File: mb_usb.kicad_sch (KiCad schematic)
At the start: 51 parts, among them J11 USB_A_Stacked, J8 USB_A_Stacked, J9 USB_C_Receptacle_USB2.0, U7 USB3320, U8 TPS2051BDBV, U9 GL850G, Y1 24Mhz, Y2 12Mhz

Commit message: update sch&layout
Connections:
- net H_DM renamed H_DN
- net H_DM1 renamed 1H_DN
- net H_DM2 renamed 2H_DN
- net H_DM3 renamed 3H_DN
- net H_DM4 renamed 4H_DN
- net H_DP1 renamed 1H_DP
- net H_DP2 renamed 2H_DP
- net H_DP3 renamed 3H_DP
- net H_DP4 renamed 4H_DP
- net S_DM renamed S_DN
- net USB_DM renamed USB_DN
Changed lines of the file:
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@@
     (stroke (width 0) (type default) (color 0 0 0 0))
   )
-  (label "H_DP4" (at 90.17 140.97 180)
+  (label "4H_DP" (at 90.17 140.97 180)
     (effects (font (size 1.27 1.27)) (justify right bottom))
   )
@@
     (effects (font (size 1.27 1.27)) (justify right bottom))
   )
-  (label "S_DM" (at 240.03 130.81 0)
+  (label "S_DN" (at 240.03 130.81 0)
     (effects (font (size 1.27 1.27)) (justify left bottom))
   )
-  (label "USB_DM" (at 151.13 70.485 180)
+  (label "USB_DN" (at 151.13 70.485 180)
     (effects (font (size 1.27 1.27)) (justify right bottom))
   )
-  (label "H_DP1" (at 90.17 121.92 180)
+  (label "1H_DP" (at 90.17 121.92 180)
     (effects (font (size 1.27 1.27)) (justify right bottom))
   )
@@
     (effects (font (size 1.27 1.27)) (justify left bottom))
   )
-  (label "H_DM" (at 130.175 70.485 0)
+  (label "H_DN" (at 130.175 70.485 0)
     (effects (font (size 1.27 1.27)) (justify left bottom))
   )
-  (label "USB_DM" (at 91.44 69.85 180)
+  (label "USB_DN" (at 91.44 69.85 180)
     (effects (font (size 1.27 1.27)) (justify right bottom))
   )
-  (label "H_DM2" (at 221.615 41.91 0)
+  (label "2H_DN" (at 221.615 41.91 0)
     (effects (font (size 1.27 1.27)) (justify left bottom))
   )
@@
     (effects (font (size 1.27 1.27)) (justify left bottom))
   )
-  (label "H_DM1" (at 221.615 36.83 0)
+  (label "1H_DN" (at 221.615 36.83 0)
     (effects (font (size 1.27 1.27)) (justify left bottom))
   )
-  (label "H_DM4" (at 90.17 143.51 180)
+  (label "4H_DN" (at 90.17 143.51 180)
     (effects (font (size 1.27 1.27)) (justify right bottom))
   )
@@
     (effects (font (size 1.27 1.27)) (justify right bottom))
   )
-  (label "S_DM" (at 130.175 64.135 0)
+  (label "S_DN" (at 130.175 64.135 0)
     (effects (font (size 1.27 1.27)) (justify left bottom))
   )
@@
     (effects (font (size 1.27 1.27)) (justify right bottom))
   )
-  (label "H_DP4" (at 220.98 88.265 0)
+  (label "4H_DP" (at 220.98 88.265 0)
     (effects (font (size 1.27 1.27)) (justify left bottom))
   )
@@
     (effects (font (size 1.27 1.27)) (justify right bottom))
   )
-  (label "H_DM" (at 52.07 124.46 0)
+  (label "H_DN" (at 52.07 124.46 0)
     (effects (font (size 1.27 1.27)) (justify left bottom))
   )
@@
     (effects (font (size 1.27 1.27)) (justify left bottom))
   )
-  (label "H_DM2" (at 90.17 130.81 180)
+  (label "2H_DN" (at 90.17 130.81 180)
     (effects (font (size 1.27 1.27)) (justify right bottom))
   )
@@
     (effects (font (size 1.27 1.27)) (justify right bottom))
   )
-  (label "H_DM1" (at 90.17 124.46 180)
+  (label "1H_DN" (at 90.17 124.46 180)
     (effects (font (size 1.27 1.27)) (justify right bottom))
   )
@@
     (effects (font (size 1.27 1.27)) (justify left bottom))
   )
-  (label "H_DM3" (at 90.17 137.16 180)
+  (label "3H_DN" (at 90.17 137.16 180)
     (effects (font (size 1.27 1.27)) (justify right bottom))
   )
@@
     (effects (font (size 1.27 1.27)) (justify right bottom))
   )
-  (label "H_DP2" (at 90.17 128.27 180)
+  (label "2H_DP" (at 90.17 128.27 180)
     (effects (font (size 1.27 1.27)) (justify right bottom))
   )
@@
     (effects (font (size 1.27 1.27)) (justify left bottom))
   )
-  (label "H_DP3" (at 220.98 83.185 0)
+  (label "3H_DP" (at 220.98 83.185 0)
     (effects (font (size 1.27 1.27)) (justify left bottom))
   )
-  (label "H_DM4" (at 220.98 90.805 0)
+  (label "4H_DN" (at 220.98 90.805 0)
     (effects (font (size 1.27 1.27)) (justify left bottom))
   )
-  (label "H_DP1" (at 221.615 34.29 0)
+  (label "1H_DP" (at 221.615 34.29 0)
     (effects (font (size 1.27 1.27)) (justify left bottom))
   )
-  (label "H_DM3" (at 220.98 85.725 0)
+  (label "3H_DN" (at 220.98 85.725 0)
     (effects (font (size 1.27 1.27)) (justify left bottom))
   )
@@
     (effects (font (size 1.27 1.27)) (justify right bottom))
   )
-  (label "H_DP3" (at 90.17 134.62 180)
+  (label "3H_DP" (at 90.17 134.62 180)
     (effects (font (size 1.27 1.27)) (justify right bottom))
   )
-  (label "H_DP2" (at 221.615 39.37 0)
+  (label "2H_DP" (at 221.615 39.37 0)
     (effects (font (size 1.27 1.27)) (justify left bottom))
   )

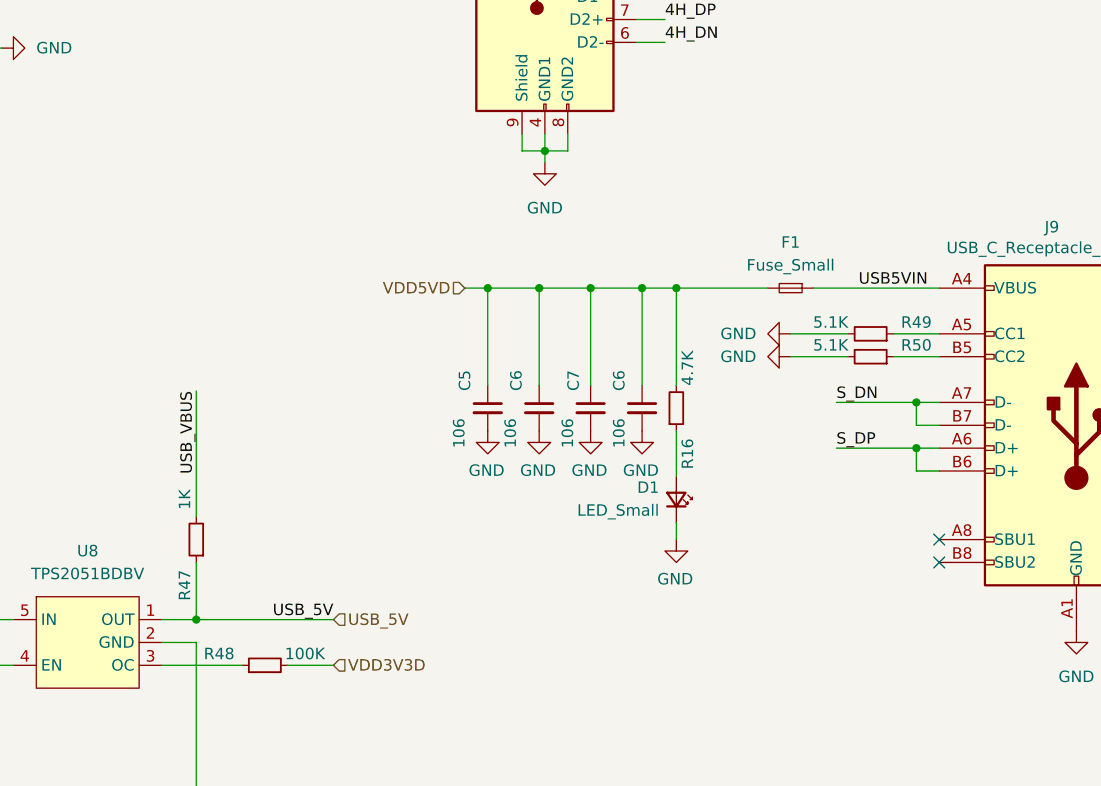
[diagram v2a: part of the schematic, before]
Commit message: Finall version --fix USB bug
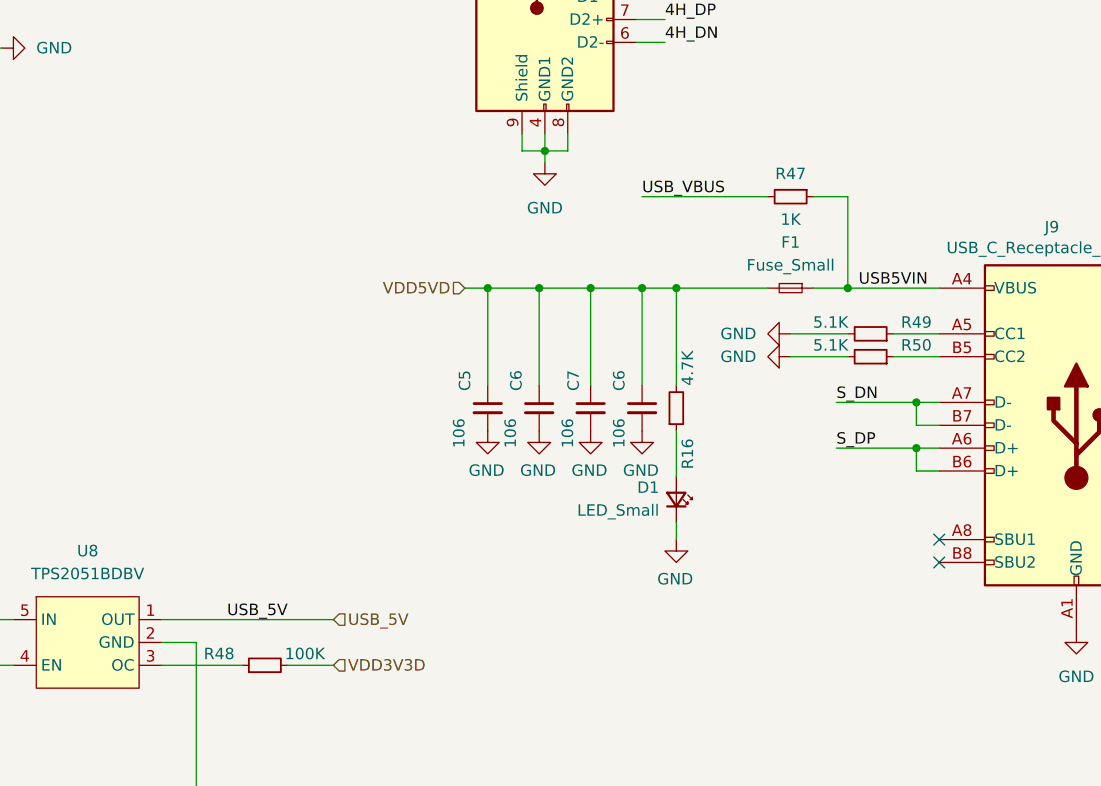
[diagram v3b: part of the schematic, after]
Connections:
- net USB5VIN: now also R47.1
- net USB_5V: no longer R47.1
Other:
- moved on the sheet: R47
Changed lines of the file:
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@@
   (junction (at 106.68 49.53) (diameter 0) (color 0 0 0 0)
   )
+  (junction (at 241.3 118.11) (diameter 0) (color 0 0 0 0)
+  )
   (junction (at 218.44 118.11) (diameter 0) (color 0 0 0 0)
   )
@@
   )
   (junction (at 41.91 167.64) (diameter 0) (color 0 0 0 0)
-  )
-  (junction (at 168.91 154.94) (diameter 0) (color 0 0 0 0)
   )
   (junction (at 55.88 134.62) (diameter 0) (color 0 0 0 0)
@@
     (stroke (width 0) (type default))
   )
+  (wire (pts (xy 241.3 118.11) (xy 251.46 118.11))
+    (stroke (width 0) (type default))
+  )
   (wire (pts (xy 106.68 49.53) (xy 109.22 49.53))
     (stroke (width 0) (type default))
@@
     (stroke (width 0) (type default))
   )
-  (wire (pts (xy 237.49 118.11) (xy 251.46 118.11))
+  (wire (pts (xy 237.49 118.11) (xy 241.3 118.11))
     (stroke (width 0) (type default))
   )
@@
     (stroke (width 0) (type default))
   )
-  (wire (pts (xy 168.91 129.54) (xy 168.91 143.51))
+  (wire (pts (xy 218.44 107.95) (xy 232.41 107.95))
     (stroke (width 0) (type default))
   )
@@
     (stroke (width 0) (type default))
   )
-  (wire (pts (xy 168.91 154.94) (xy 165.1 154.94))
-    (stroke (width 0) (type default))
-  )
   (wire (pts (xy 90.17 166.37) (xy 83.82 166.37))
     (stroke (width 0) (type default))
@@
     (stroke (width 0) (type default))
   )
-  (wire (pts (xy 168.91 154.94) (xy 184.15 154.94))
+  (wire (pts (xy 165.1 154.94) (xy 184.15 154.94))
     (stroke (width 0) (type default))
   )
@@
     (stroke (width 0) (type default))
   )
+  (wire (pts (xy 237.49 107.95) (xy 241.3 107.95))
+    (stroke (width 0) (type default))
+  )
   (wire (pts (xy 53.34 151.13) (xy 57.15 151.13))
     (stroke (width 0) (type default))
@@
     (stroke (width 0) (type default))
   )
-  (wire (pts (xy 168.91 148.59) (xy 168.91 154.94))
-    (stroke (width 0) (type default))
-  )
   (wire (pts (xy 29.21 85.09) (xy 33.02 85.09))
     (stroke (width 0) (type default))
@@
   )
   (wire (pts (xy 88.9 100.33) (xy 88.9 104.14))
+    (stroke (width 0) (type default))
+  )
+  (wire (pts (xy 241.3 107.95) (xy 241.3 118.11))
     (stroke (width 0) (type default))
   )
@@
     (effects (font (size 1.27 1.27)) (justify right bottom))
   )
-  (label "USB_5V" (at 184.15 154.94 180) (fields_autoplaced)
+  (label "USB_5V" (at 179.07 154.94 180) (fields_autoplaced)
     (effects (font (size 1.27 1.27)) (justify right bottom))
   )
@@
     (effects (font (size 1.27 1.27)) (justify right bottom))
   )
-  (label "USB_VBUS" (at 168.91 129.54 270) (fields_autoplaced)
-    (effects (font (size 1.27 1.27)) (justify right bottom))
+  (label "USB_VBUS" (at 218.44 107.95 0) (fields_autoplaced)
+    (effects (font (size 1.27 1.27)) (justify left bottom))
   )
   (label "USB_ID" (at 91.44 76.2 180) (fields_autoplaced)
@@
     )
   )
-  (symbol (lib_id "Device:R_Small") (at 168.91 146.05 180) (unit 1)
-    (in_bom yes) (on_board yes) (dnp no)
-    (property "Reference" "R47" (at 167.64 151.13 90)
-      (effects (font (size 1.27 1.27)))
-    )
-    (property "Value" "1K" (at 167.64 141.605 90)
-      (effects (font (size 1.27 1.27)))
-    )
-    (property "Footprint" "Resistor_SMD:R_0402_1005Metric" (at 168.91 146.05 0)
-      (effects (font (size 1.27 1.27)) hide)
-    )
-    (property "Datasheet" "~" (at 168.91 146.05 0)
-      (effects (font (size 1.27 1.27)) hide)
-    )
+  (symbol (lib_id "Device:R_Small") (at 234.95 107.95 270) (unit 1)
+    (in_bom yes) (on_board yes) (dnp no)
+    (property "Reference" "R47" (at 234.95 105.41 90)
+      (effects (font (size 1.27 1.27)))
+    )
+    (property "Value" "1K" (at 234.95 110.49 90)
+      (effects (font (size 1.27 1.27)))
+    )
+    (property "Footprint" "Resistor_SMD:R_0402_1005Metric" (at 234.95 107.95 0)
+      (effects (font (size 1.27 1.27)) hide)
+    )
+    (property "Datasheet" "~" (at 234.95 107.95 0)
+      (effects (font (size 1.27 1.27)) hide)
+    )
